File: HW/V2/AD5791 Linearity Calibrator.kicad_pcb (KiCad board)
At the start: 4 copper layers, 100 x 100 mm, 21 parts, among them J7 Conn_01x32, U1 7533, U2 L78L15, U3 L79L15

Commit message: v2
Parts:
- removed J5, J6: ~, 100mm template footprints:CTB93HD3
- added ?: , , F.Cu at (161.0, 146.5)
- added ?: , , F.Cu at (79.0, 53.5)
- added ?: , , F.Cu at (161.0, 53.5)
- added C10: 100nF, Capacitor_SMD:C_0603_1608Metric, F.Cu at (110.2, 101.5)
- added C11: 100nF, Capacitor_SMD:C_0603_1608Metric, F.Cu at (110.2, 104.0)
- added C12: 100nF, Capacitor_SMD:C_0603_1608Metric, F.Cu at (110.2, 106.5)
- added C13: 100nF, Capacitor_SMD:C_0603_1608Metric, F.Cu at (114.2, 99.0)
- added C14: 100nF, Capacitor_SMD:C_0603_1608Metric, F.Cu at (114.2, 101.5)
- added C4: 100nF, Capacitor_SMD:C_0603_1608Metric, F.Cu at (89.5, 126.8)
- added C5: 10uF, Resistor_SMD:R_0603_1608Metric, F.Cu at (135.6, 80.2)
- added C6: 10uF, Resistor_SMD:R_0603_1608Metric, F.Cu at (135.6, 82.7)
- added C7: 10uF, Resistor_SMD:R_0603_1608Metric, F.Cu at (135.6, 85.2)
- added C8: 10pF, Resistor_SMD:R_0603_1608Metric, F.Cu at (143.8, 97.5)
- added C9: 100nF, Capacitor_SMD:C_0603_1608Metric, F.Cu at (110.2, 99.0)
- added D1: 5819, Resistor_SMD:R_0603_1608Metric_Pad0.98x0.95mm_HandSolder, F.Cu at (140.2, 82.8)
- added D2: 5819, Resistor_SMD:R_0603_1608Metric_Pad0.98x0.95mm_HandSolder, F.Cu at (149.1, 91.0)
- added H1: MountingHole_Pad, MountingHole:MountingHole_3.2mm_M3_Pad_Via, F.Cu at (80.5, 125.0)
- added H2: MountingHole_Pad, MountingHole:MountingHole_3.2mm_M3_Pad_Via, F.Cu at (110.5, 125.0)
- added R1: 10R, Resistor_SMD:R_0603_1608Metric, F.Cu at (89.5, 123.4)
- added R2: 10R, Resistor_SMD:R_0603_1608Metric, F.Cu at (114.2, 104.0)
- added R3: 10R, Resistor_SMD:R_0603_1608Metric, F.Cu at (114.2, 106.5)
- added R4: 10R, Resistor_SMD:R_0603_1608Metric, F.Cu at (118.2, 99.0)
- added R5: 10R, Resistor_SMD:R_0603_1608Metric, F.Cu at (118.2, 101.5)
- added R6: 10R, Resistor_SMD:R_0603_1608Metric, F.Cu at (118.2, 104.0)
- added R7: 10R, Resistor_SMD:R_0603_1608Metric, F.Cu at (118.2, 106.5)
- added REF**: MountingHole_3.2mm_M3_DIN965_Pad, MountingHole:MountingHole_3.2mm_M3_DIN965_Pad, F.Cu at (79.0, 146.5)
- added SW1: RST, Button_Switch_SMD:SW_SPST_B3U-1000P, F.Cu at (149.8, 87.6)
- added U4: LT1021, Package_DIP:DIP-8_W7.62mm, F.Cu at (91.7, 121.7)
- added U5: AD5791BRUZ, AD5791BRUZ:SOP65P640X120-20N, F.Cu at (138.0, 105.0)
- added U6: +BUFF, Package_SO:SOIC-8_3.9x4.9mm_P1.27mm, F.Cu at (129.8, 105.0)
- added U7: -BUFF, Package_SO:SOIC-8_3.9x4.9mm_P1.27mm, F.Cu at (147.0, 105.2)
- added U8: Pico, MCU_RaspberryPi_and_Boards:RPi_Pico_SMD_TH, F.Cu at (144.5, 126.0)
- added U9: OBUFF, Package_SO:SOIC-8_3.9x4.9mm_P1.27mm, F.Cu at (138.2, 98.0)
- moved C1 11.0 mm to (151.0, 57.5)
- moved U1 11.0 mm to (151.0, 67.5)
- moved U2 11.0 mm to (141.0, 67.4)
- moved U3 11.0 mm to (131.0, 67.5)
- moved C2 10.8 mm to (141.0, 57.5)
- moved C3 10.8 mm to (131.0, 57.5)
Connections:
- net Net-(U1-VIN) renamed +15V
- net Net-(U1-VOUT) renamed +3.3V
- net Net-(U3-VO) renamed -15V
- J1 pad 1: unconnected-(J1-Pin_1-Pad1) -> Net-(J1-Pin_1)
- J1 pad 2: unconnected-(J1-Pin_2-Pad2) -> GND
- J1 pad 3: unconnected-(J1-Pin_3-Pad3) -> Net-(J1-Pin_3)
- U2 pad 3: unconnected-(U2-IN-Pad3) -> Net-(J1-Pin_3)
- U3 pad 2: unconnected-(U3-VI-Pad2) -> Net-(J1-Pin_1)
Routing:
- net Net-(U4-IN): track 0.00 -> 3.94 mm
- net GND: track 0.00 -> 0.97 mm, vias 15 -> 19
- net +15V: track 0.00 -> 0.84 mm, vias 15 -> 18
- net unconnected-(U3-VI-Pad2): vias 15 -> 0
- net Net-(J1-Pin_3): vias 0 -> 1
- net Net-(J1-Pin_1): vias 0 -> 16
- net -15V: vias 0 -> 1
- net +3.3V: vias 0 -> 1
- added copper zone on B.Cu, net (none)
- added copper zone on F.Cu, net (none)
- added copper zone on B.Cu, net Net-(J1-Pin_1)
- added copper zone on F.Cu, net Net-(J1-Pin_1)
- added copper zone on In1.Cu, net Net-(J1-Pin_1)
- added copper zone on In2.Cu, net Net-(J1-Pin_1)
- added copper zone on F.Cu, net Net-(J1-Pin_3)
- removed copper zone on F.Cu, net unconnected-(U2-IN-Pad3)
- removed copper zone on B.Cu, net unconnected-(U3-VI-Pad2)
- removed copper zone on F.Cu, net unconnected-(U3-VI-Pad2)
- removed copper zone on In1.Cu, net unconnected-(U3-VI-Pad2)
- removed copper zone on In2.Cu, net unconnected-(U3-VI-Pad2)
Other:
- outline, holes or cut-outs redrawn

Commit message: finalized schematics for v2
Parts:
- removed U4: LT1021, Package_DIP:DIP-8_W7.62mm
- added D3: 5819, Resistor_SMD:R_0603_1608Metric_Pad0.98x0.95mm_HandSolder, F.Cu at (89.9, 106.5)
- added JP1: DACOUT, Connector_PinHeader_2.54mm:PinHeader_1x02_P2.54mm_Vertical, F.Cu at (101.0, 106.8)
- added R8: 1K, Resistor_SMD:R_0603_1608Metric, F.Cu at (85.8, 106.5)
- added R9: 5R1, Resistor_SMD:R_0603_1608Metric, F.Cu at (85.8, 109.0)
- added RN1: 10K, Package_SO:SOIC-16_3.9x9.9mm_P1.27mm, F.Cu at (101.0, 97.9)
- added U10: ADR1399, Package_TO_SOT_THT:Analog_TO-46-4_ThermalShield, F.Cu at (94.2, 126.5)
- C4: value 100nF -> 1uF; footprint Capacitor_SMD:C_0603_1608Metric -> Resistor_SMD:R_0603_1608Metric
- C8: value 10pF -> 1uF
- R1: value 10R -> 100K
- U6: value +BUFF -> REFSCALE
- U7: value -BUFF -> REFBUF
- U9: value OBUFF -> OUTBUF
- moved SW1 54.3 mm to (143.2, 141.5), turned to 90 degrees
- moved U6 46.4 mm to (102.5, 67.5), turned to 0 degrees
- moved U9 41.0 mm to (102.0, 78.8)
- moved C12 40.5 mm to (96.8, 68.2)
- moved R2 38.9 mm to (108.2, 65.5), turned to 180 degrees
- moved R5 38.5 mm to (96.8, 69.5)
- moved R7 34.8 mm to (96.2, 79.5)
- moved C9 32.3 mm to (108.2, 66.8), turned to 180 degrees
- moved U7 29.9 mm to (125.0, 85.0), turned to 0 degrees
- moved R3 28.8 mm to (130.8, 83.0), turned to 180 degrees
- moved C14 27.4 mm to (96.2, 80.8)
- moved C10 26.9 mm to (130.8, 84.2), turned to 180 degrees
- moved C11 26.1 mm to (107.8, 78.0), turned to 180 degrees
- moved R4 24.5 mm to (107.8, 76.8), turned to 180 degrees
- moved R1 19.0 mm to (82.0, 106.0)
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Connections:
- C10 pad 2: Net-(U7A-V+) -> Net-(U9C-V+)
- C11 pad 2: Net-(U9A-V+) -> Net-(U6C-V+)
- C12 pad 2: Net-(U6A-V-) -> Net-(U7C-V-)
- C13 pad 2: Net-(U7A-V-) -> Net-(U9C-V-)
- C14 pad 2: Net-(U9A-V-) -> Net-(U6C-V-)
- C4 pad 1: GND -> +15V
- C4 pad 2: Net-(U4-IN) -> -15V
- C8 pad 1: Net-(U5-RFB) -> Net-(C8-Pad1)
- C8 pad 2: Net-(U5-INV) -> GNDA
- C9 pad 2: Net-(U6A-V+) -> Net-(U7C-V+)
- R1 pad 2: Net-(U4-IN) -> /7VREF
- R2 pad 2: Net-(U6A-V+) -> Net-(U7C-V+)
- R3 pad 2: Net-(U7A-V+) -> Net-(U9C-V+)
- R4 pad 2: Net-(U9A-V+) -> Net-(U6C-V+)
- R5 pad 2: Net-(U6A-V-) -> Net-(U7C-V-)
- R6 pad 2: Net-(U7A-V-) -> Net-(U9C-V-)
- R7 pad 2: Net-(U9A-V-) -> Net-(U6C-V-)
- U5 pad 1: Net-(U5-INV) -> unconnected-(U5-INV-Pad1)
- U5 pad 2: Net-(U5-VOUT) -> Net-(JP1-A)
- U5 pad 20: Net-(U5-RFB) -> unconnected-(U5-RFB-Pad20)
- U6 pad 1: unconnected-(U6A-VOS-Pad1) -> /+10.5V
- U6 pad 2: /VREFPS -> Net-(RN1D-R4.1)
- U6 pad 3: /10VREF -> /7VREF
- U6 pad 4: Net-(U6A-V-) -> Net-(U6C-V-)
- U6 pad 5: unconnected-(U6A-NC-Pad5) -> GND
- U6 pad 6: /VREFPF -> Net-(RN1G-R7.1)
- U6 pad 7: Net-(U6A-V+) -> /-10.5V
- U6 pad 8: unconnected-(U6A-VOS-Pad8) -> Net-(U6C-V+)
- U7 pad 1: unconnected-(U7A-VOS-Pad1) -> /VREFPF
- U7 pad 2: /VREFNS -> /VREFPS
- U7 pad 3: GND -> /+10.5V
- U7 pad 4: Net-(U7A-V-) -> Net-(U7C-V-)
- U7 pad 5: unconnected-(U7A-NC-Pad5) -> /-10.5V
- U7 pad 6: /VREFNF -> /VREFNS
- U7 pad 7: Net-(U7A-V+) -> /VREFNF
- U7 pad 8: unconnected-(U7A-VOS-Pad8) -> Net-(U7C-V+)
- U8 pad 39: Net-(D2-A) -> unconnected-(U8-VSYS-Pad39)
- U8 pad 40: unconnected-(U8-VBUS-Pad40) -> Net-(D2-A)
- U9 pad 1: unconnected-(U9A-VOS-Pad1) -> Net-(U9A--)
- U9 pad 2: Net-(U5-INV) -> Net-(U9A--)
- U9 pad 3: Net-(U5-VOUT) -> Net-(JP1-B)
- U9 pad 4: Net-(U9A-V-) -> Net-(U9C-V-)
- U9 pad 5: unconnected-(U9A-NC-Pad5) -> GNDA
- U9 pad 6: Net-(U5-RFB) -> Net-(U9B--)
- U9 pad 7: Net-(U9A-V+) -> Net-(U9B--)
- U9 pad 8: unconnected-(U9A-VOS-Pad8) -> Net-(U9C-V+)
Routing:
- net /VREFPF: track 0.00 -> 11.9 mm
- net /VREFNF: track 0.00 -> 11.1 mm
- net /VREFPS: track 0.00 -> 9.51 mm
- net /VREFNS: track 0.00 -> 8.81 mm
- net Net-(U4-IN): track 3.94 -> 0.00 mm
- net GND: track 0.97 -> 0.00 mm, vias 19 -> 18
- net +15V: track 0.84 -> 0.00 mm, vias 18 -> 17
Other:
- outline, holes or cut-outs redrawn

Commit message: updated v2 PCB files
finalized layout?
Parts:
- removed D2: 5819, Resistor_SMD:R_0603_1608Metric_Pad0.98x0.95mm_HandSolder
- removed J2, J3: ~, 100mm template footprints:CTB93HD3
- removed J7: Conn_01x32, 100mm template footprints:SIL32
- added JP2: DACOUT, Connector_PinHeader_1.27mm:PinHeader_1x02_P1.27mm_Vertical, F.Cu at (157.0, 97.6)
- added R10: 220R, Resistor_SMD:R_0603_1608Metric, F.Cu at (131.8, 64.8)
- added R11: 2K4, Resistor_SMD:R_0603_1608Metric, F.Cu at (128.2, 64.8)
- added R12: 220R, Resistor_SMD:R_0603_1608Metric, F.Cu at (88.2, 64.8)
- added R13: 2K4, Resistor_SMD:R_0603_1608Metric, F.Cu at (91.8, 64.8)
- added R14: 220R, Resistor_SMD:R_0603_1608Metric, F.Cu at (108.2, 64.8)
- added R15: 390R, Resistor_SMD:R_0603_1608Metric, F.Cu at (111.8, 64.8)
- C4, C5, C6, C7, C8: footprint Resistor_SMD:R_0603_1608Metric -> Capacitor_SMD:C_0603_1608Metric
- H1, H2: footprint MountingHole:MountingHole_3.2mm_M3_Pad_Via -> MountingHole:MountingHole_3.2mm_M3_DIN965_Pad
- JP1: footprint Connector_PinHeader_2.54mm:PinHeader_1x02_P2.54mm_Vertical -> Connector_PinHeader_1.27mm:PinHeader_1x02_P1.27mm_Vertical
- U1: value 7533 -> LM317; footprint Package_TO_SOT_SMD:SOT-89-3 -> Package_TO_SOT_SMD:TO-252-2
- U2: value L78L15 -> LM337; footprint Package_TO_SOT_SMD:SOT-89-3 -> Package_TO_SOT_SMD:TO-252-2
- U3: value L79L15 -> LM317; footprint Package_TO_SOT_SMD:SOT-89-3 -> Package_TO_SOT_SMD:TO-252-2
- moved U2 50.4 mm to (90.0, 73.3)
- moved C12 45.6 mm to (122.8, 105.8), turned to 90 degrees
- moved R5 45.4 mm to (124.0, 105.8), turned to 90 degrees
- moved C8 44.9 mm to (99.0, 94.2), turned to 90 degrees
- moved C1 41.1 mm to (110.0, 60.0)
- moved U9 40.9 mm to (137.0, 100.0), turned to 90 degrees
- moved C3 39.1 mm to (90.0, 60.0)
- moved H1 37.2 mm to (90.0, 90.0)
- moved U6 32.5 mm to (104.0, 100.0), turned to -90 degrees
- moved R2 31.6 mm to (121.2, 94.2), turned to -90 degrees
- moved D1 30.6 mm to (130.5, 105.8), turned to 90 degrees
- moved C9 29.9 mm to (120.0, 94.2), turned to -90 degrees
- moved C5 29.2 mm to (132.0, 105.8), turned to -90 degrees
- moved R4 29.2 mm to (104.8, 105.8), turned to 90 degrees
- moved C6 28.7 mm to (129.0, 105.8), turned to -90 degrees
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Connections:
- D3 pad 2: /VREFPF -> /+10.5V
- J4 pad 1: unconnected-(J4-Pin_1-Pad1) -> Net-(J4-Pin_1)
- J4 pad 2: unconnected-(J4-Pin_2-Pad2) -> GNDA
- J4 pad 3: unconnected-(J4-Pin_3-Pad3) -> Net-(J4-Pin_3)
- JP1 pad 1: Net-(JP1-A) -> /BUFIN
- JP1 pad 2: Net-(JP1-B) -> /BUFIN
- RN1 pad 10: Net-(RN1E-R5.1) -> Net-(RN1F-R6.1)
- RN1 pad 11: Net-(RN1C-R3.1) -> Net-(RN1E-R5.2)
- RN1 pad 12: Net-(RN1D-R4.1) -> Net-(RN1E-R5.2)
- RN1 pad 13: /+10.5V -> Net-(RN1C-R3.2)
- RN1 pad 14: /-10.5V -> Net-(RN1C-R3.2)
- RN1 pad 15: unconnected-(RN1B-R2.2-Pad15) -> /+10.5V
- RN1 pad 2: unconnected-(RN1B-R2.1-Pad2) -> Net-(RN1B-R2.1)
- RN1 pad 3: Net-(RN1C-R3.1) -> Net-(RN1B-R2.1)
- RN1 pad 5: Net-(RN1E-R5.1) -> Net-(RN1D-R4.1)
- RN1 pad 7: Net-(RN1G-R7.1) -> /-10.5V
- RN1 pad 8: Net-(RN1G-R7.1) -> unconnected-(RN1H-R8.1-Pad8)
- RN1 pad 9: Net-(RN1F-R6.1) -> unconnected-(RN1H-R8.2-Pad9)
- U1 pad 1: GND -> Net-(U1-ADJ)
- U1 pad 3: +3.3V -> Net-(J1-Pin_3)
- U2 pad 1: +15V -> Net-(U2-ADJ)
- U2 pad 2: GND -> Net-(J1-Pin_1)
- U2 pad 3: Net-(J1-Pin_3) -> -15V
- U3 pad 1: GND -> Net-(U3-ADJ)
- U3 pad 2: Net-(J1-Pin_1) -> +3.3V
- U3 pad 3: -15V -> +15V
- U5 pad 2: Net-(JP1-A) -> /BUFIN
- U6 pad 1: /+10.5V -> /-10.5V
- U6 pad 3: /7VREF -> GNDA
- U6 pad 5: GND -> /7VREF
- U6 pad 6: Net-(RN1G-R7.1) -> Net-(RN1B-R2.1)
- U6 pad 7: /-10.5V -> /+10.5V
- U8 pad 40: Net-(D2-A) -> unconnected-(U8-VBUS-Pad40)
- U9 pad 1: Net-(U9A--) -> Net-(J4-Pin_1)
- U9 pad 2: Net-(U9A--) -> Net-(J4-Pin_1)
- U9 pad 3: Net-(JP1-B) -> /BUFIN
- U9 pad 6: Net-(U9B--) -> Net-(J4-Pin_3)
- U9 pad 7: Net-(U9B--) -> Net-(J4-Pin_3)
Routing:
- net /7VREF: track 0.00 -> 28.8 mm, vias 0 -> 1
- net GNDA: track 0.00 -> 25.2 mm, vias 0 -> 2
- net Net-(RN1B-R2.1): track 0.00 -> 24.4 mm
- net /+10.5V: track 0.00 -> 21.2 mm, vias 0 -> 2
- net Net-(RN1D-R4.1): track 0.00 -> 16.2 mm
- net +15V: track 0.00 -> 13.1 mm, vias 17 -> 18
- net Net-(RN1F-R6.1): track 0.00 -> 12.3 mm, vias 0 -> 2
- net -15V: track 0.00 -> 11.2 mm, vias 1 -> 3
- net /-10.5V: track 0.00 -> 9.92 mm, vias 0 -> 2
- net GND: track 0.00 -> 8.77 mm, vias 18 -> 9
- net /BUFIN: track 0.00 -> 7.01 mm
- net Net-(RN1E-R5.2): track 0.00 -> 4.32 mm
- net Net-(RN1C-R3.2): track 0.00 -> 4.32 mm
- net Net-(U6C-V-): track 0.00 -> 3.81 mm
- net Net-(D3-K): track 0.00 -> 1.54 mm
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- added copper zone on In1.Cu, net (none)
- added copper zone on In2.Cu, net (none)
- added copper zone on B.Cu, net +3.3V
- added copper zone on In1.Cu, net +3.3V
- added copper zone on In2.Cu, net +3.3V
- removed copper zone on F.Cu, net -15V
- removed copper zone on B.Cu, net GND
- removed copper zone on F.Cu, net GND
- removed copper zone on In1.Cu, net GND
- removed copper zone on In2.Cu, net GND
- removed copper zone on F.Cu, net Net-(J1-Pin_3)
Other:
- board size 100 x 100 mm -> 80 x 100 mm

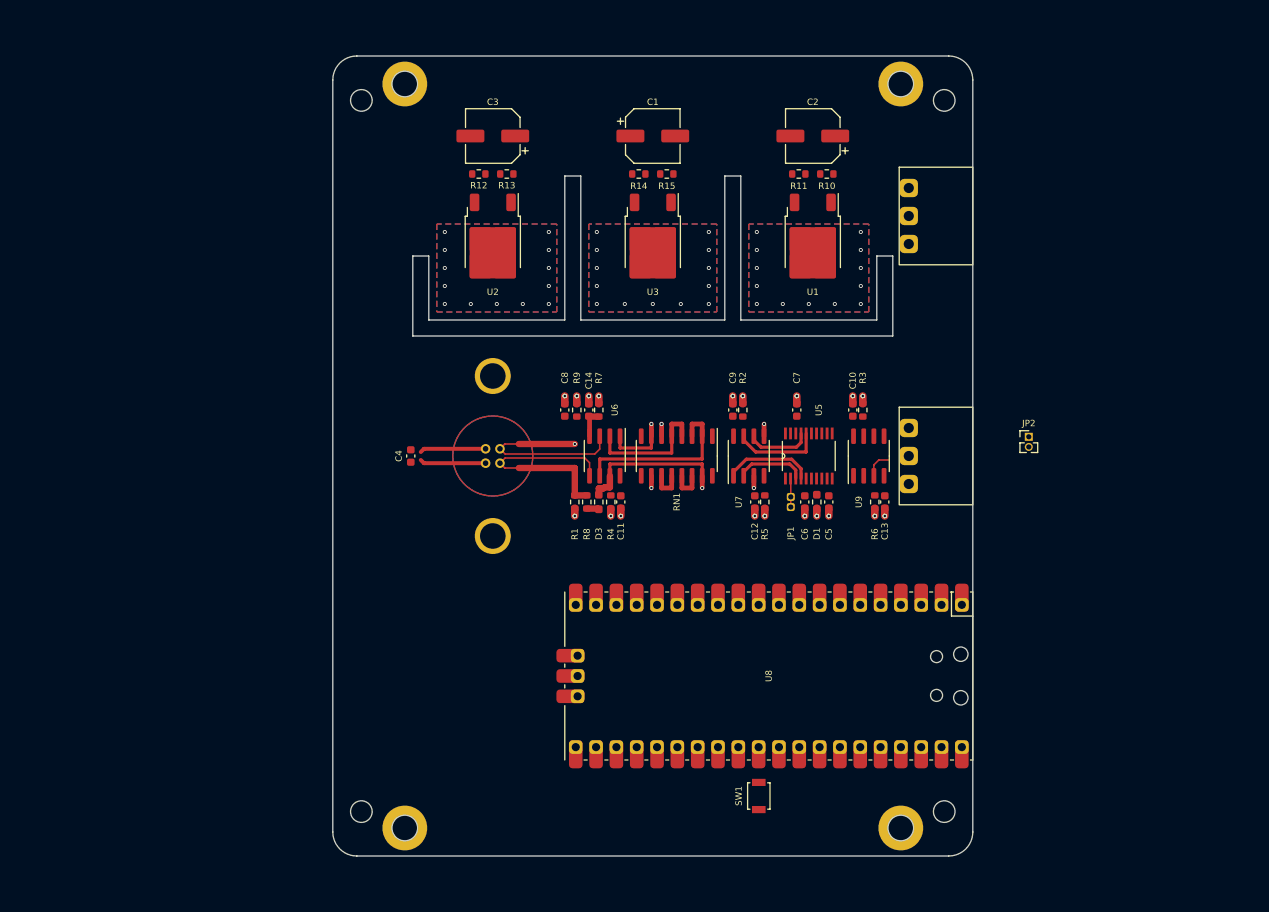
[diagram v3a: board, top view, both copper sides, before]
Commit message: updated v2 layout
added isolator, artwork, finalized placement
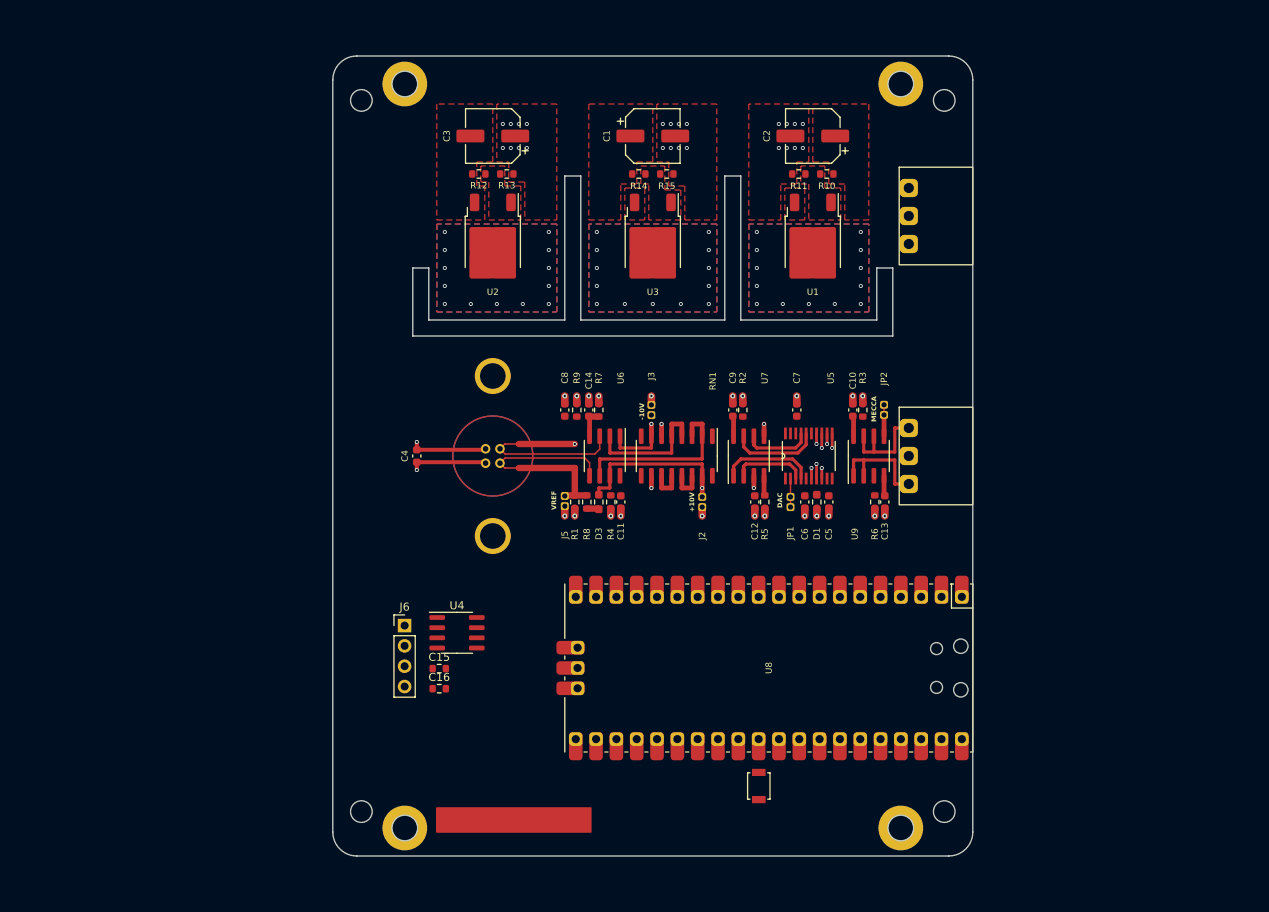
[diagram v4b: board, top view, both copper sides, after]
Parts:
- added C15: 10uF, Resistor_SMD:R_0603_1608Metric, F.Cu at (83.3, 126.6)
- added C16: 10uF, Resistor_SMD:R_0603_1608Metric, F.Cu at (83.3, 129.1)
- added J2: VREFP, Connector_PinHeader_1.27mm:PinHeader_1x02_P1.27mm_Vertical, F.Cu at (116.2, 105.1)
- added J3: VREFN, Connector_PinHeader_1.27mm:PinHeader_1x02_P1.27mm_Vertical, F.Cu at (109.8, 94.9)
- added J5: VREFP, Connector_PinHeader_1.27mm:PinHeader_1x02_P1.27mm_Vertical, F.Cu at (99.0, 105.0)
- added J6: ISO OUT, Connector_PinHeader_2.54mm:PinHeader_1x04_P2.54mm_Vertical, F.Cu at (79.0, 121.2)
- added REF**: LOGO, LOGO, B.Cu at (112.0, 126.8)
- added U4: ADuM1201AR, Package_SO:SOIC-8_3.9x4.9mm_P1.27mm, F.Cu at (85.5, 122.1)
- JP2: value DACOUT -> MECCA
- moved JP2 18.3 mm to (138.9, 94.9), turned to 180 degrees
- moved SW1 1.25 mm to (123.2, 141.2)
- moved U8 1.00 mm to (124.5, 126.5)
- moved C4 0.75 mm to (80.5, 100.0)
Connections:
- U9 pad 1: Net-(J4-Pin_1) -> Net-(J4-Pin_3)
- U9 pad 2: Net-(J4-Pin_1) -> Net-(J4-Pin_3)
- U9 pad 6: Net-(J4-Pin_3) -> Net-(J4-Pin_1)
- U9 pad 7: Net-(J4-Pin_3) -> Net-(J4-Pin_1)
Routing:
- net /-10.5V: track 9.92 -> 26.2 mm
- net Net-(J4-Pin_3): track 0.00 -> 13.9 mm
- net Net-(J4-Pin_1): track 0.00 -> 12.6 mm
- net /+10.5V: track 21.2 -> 28.9 mm
- net /BUFIN: track 7.01 -> 3.53 mm
- net GND: track 8.77 -> 12.2 mm, vias 9 -> 36
- net GNDA: track 25.2 -> 27.8 mm
- net Net-(U9C-V-): track 0.00 -> 2.54 mm
- net Net-(U9C-V+): track 0.00 -> 2.54 mm
- net Net-(U7C-V+): track 0.00 -> 2.54 mm
- net Net-(U7C-V-): track 0.00 -> 2.49 mm
- net /~{CLR}: track 0.00 -> 1.82 mm, vias 0 -> 1
- net /SDO: track 0.00 -> 1.82 mm, vias 0 -> 1
- net /SCLK: track 0.00 -> 1.82 mm, vias 0 -> 1
- net -15V: track 11.2 -> 12.6 mm, vias 3 -> 4
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- added copper zone on F.Cu, net -15V
- added copper zone on F.Cu, net GND
- added copper zone on F.Cu, net Net-(J1-Pin_3)
- added copper zone on F.Cu, net Net-(U1-ADJ)
- added copper zone on F.Cu, net Net-(U2-ADJ)
- added copper zone on F.Cu, net Net-(U3-ADJ)
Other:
- outline, holes or cut-outs redrawn
- board text added: "+10V"
- board text added: "-10V"
- board text added: "AD5791 LINEARITY CALIBRATOR NNNI 4123"
- board text added: "CLEAR ALL FLUX!"
- board text added: "DAC"
- board text added: "MECCA"
- board text added: "VREF"

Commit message: updated files
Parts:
- added J7: PWR, Connector_PinHeader_2.54mm:PinHeader_1x04_P2.54mm_Vertical, F.Cu at (73.5, 96.2)
- moved C16 12.0 mm to (91.9, 120.8), turned to 90 degrees
- moved C15 10.3 mm to (91.9, 132.2), turned to -90 degrees
- moved U4 6.28 mm to (90.0, 126.5), turned to -90 degrees
- moved J6 5.68 mm to (73.5, 122.7)
- moved R4 2.00 mm to (106.8, 105.8)
- moved R1 1.34 mm to (101.6, 105.8)
- moved R8 1.11 mm to (102.9, 105.8)
- moved J5 1.01 mm to (100.0, 105.1)
- moved D3 0.89 mm to (104.1, 105.8)
- moved C7 0.63 mm to (127.4, 94.2)
- moved R6 0.62 mm to (137.1, 105.8)
- moved C12 0.61 mm to (122.1, 105.8)
- moved C11 0.59 mm to (105.4, 105.8)
- moved C13 0.59 mm to (138.4, 105.8)
- moved R5 0.59 mm to (123.4, 105.8)
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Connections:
- J6 pad 1: /ISO_VDD -> /ISO_GND
- J6 pad 2: /ISO_TX -> /ISO_RX
- J6 pad 3: /ISO_RX -> /ISO_TX
- J6 pad 4: /ISO_GND -> /ISO_VDD
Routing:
- net /BUFIN: track 3.53 -> 22.2 mm, vias 0 -> 1
- net +3.3V: track 0.00 -> 11.5 mm, vias 13 -> 23
- net +15V: track 14.5 -> 18.8 mm, vias 19 -> 30
- net Net-(U6C-V+): track 0.00 -> 2.50 mm
- net /ISO_VDD: track 0.00 -> 2.45 mm
- net -15V: track 12.6 -> 14.7 mm, vias 4 -> 15
- net /+10.5V: track 28.9 -> 27.5 mm
- net /ISO_GND: track 0.00 -> 0.92 mm, vias 0 -> 1
- net GND: track 12.2 -> 13.0 mm, vias 36 -> 37
- net /7VREF: track 30.1 -> 29.4 mm
- net Net-(J4-Pin_3): track 13.9 -> 14.4 mm
- net Net-(J4-Pin_1): track 12.6 -> 13.1 mm
- net GNDA: track 27.8 -> 28.3 mm, vias 2 -> 3
- net Net-(J1-Pin_3): vias 0 -> 2
- added copper zone on In2.Cu, net Net-(J1-Pin_3)
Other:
- board text added: "+15"
- board text added: "+3.3"
- board text added: "-15"
- board text added: "AD5791 LINEARITY CALIBRATOR v2 NNNI 4123"
- board text added: "CLEAN ALL FLUX!"
- board text added: "GND"
- board text removed: "AD5791 LINEARITY CALIBRATOR NNNI 4123"
- board text removed: "CLEAR ALL FLUX!"
